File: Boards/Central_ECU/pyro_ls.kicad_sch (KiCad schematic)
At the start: 9 parts, among them Q2 DMT12H060LFDF-7

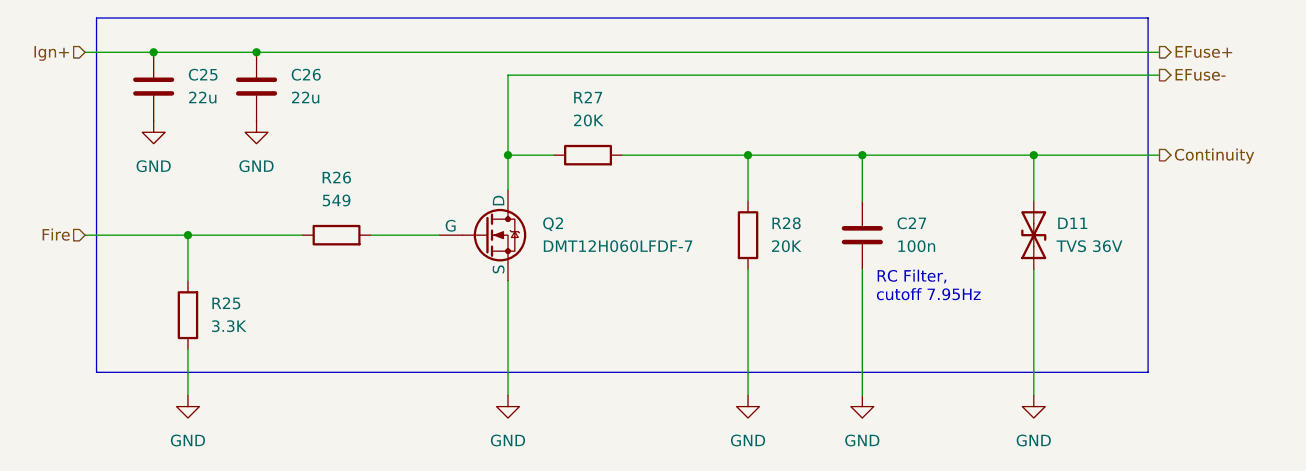
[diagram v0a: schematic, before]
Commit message: Added most connectors and hooking up
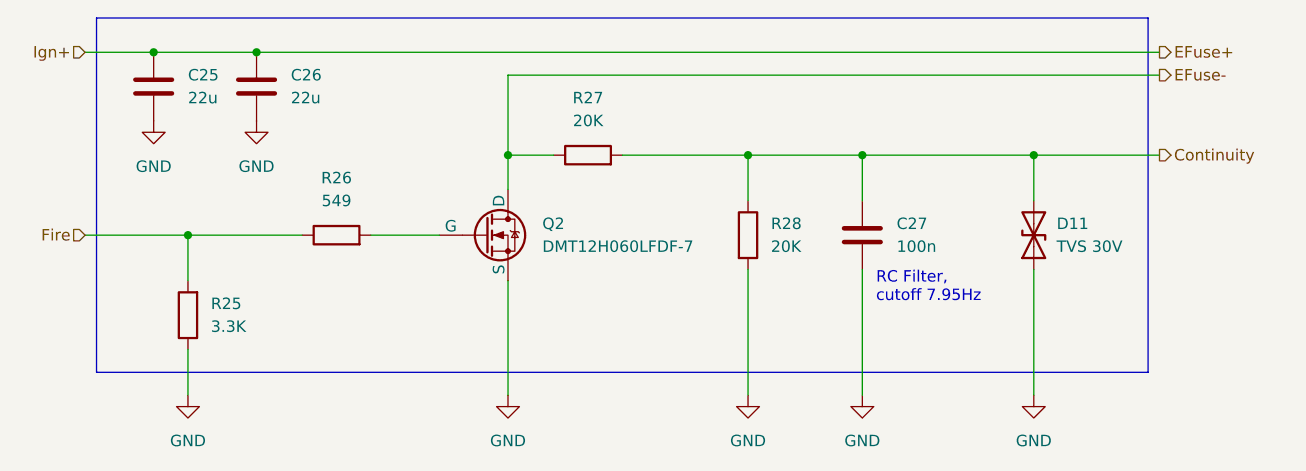
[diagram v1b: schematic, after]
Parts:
- D11: value TVS 36V -> TVS 30V; footprint Diode_SMD:D_SOD-523 -> Diode_SMD:D_SOD-882; MPN PJSD36TS_R1_00001 -> PESD1CANFD30LS-QYL
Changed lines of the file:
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@@
 			)
 		)
-		(property "Value" "TVS 36V"
+		(property "Value" "TVS 30V"
 			(at 259.08 143.51 90)
 			(effects
@@
 			)
 		)
-		(property "Footprint" "Diode_SMD:D_SOD-523"
+		(property "Footprint" "Diode_SMD:D_SOD-882"
 			(at 256.54 142.24 0)
 			(effects
@@
 			)
 		)
-		(property "Datasheet" "https://www.digikey.co.nz/en/products/detail/panjit-international-inc/PJSD36TS-R1-00001/14660198"
+		(property "Datasheet" "https://assets.nexperia.com/documents/data-sheet/PESD1CANFD30LS-Q.pdf"
 			(at 256.54 142.24 0)
 			(effects
@@
 			)
 		)
-		(property "MPN" "PJSD36TS_R1_00001"
+		(property "MPN" "PESD1CANFD30LS-QYL"
 			(at 256.54 142.24 90)
 			(effects

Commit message: For review
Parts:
- removed Q2: DMT12H060LFDF-7, Package_DFN_QFN:Diodes_UDFN2020-6_Type-F, symbol Simulation_SPICE:NMOS
- added Q2: DMT12H060LFDF, Package_DFN_QFN:Diodes_UDFN2020-6_Type-F, symbol TS_Symbols:DMT12H060LFDF
- D7: renamed from D11; MPN PESD1CANFD30LS-QYL -> PESD1CANFD30L-QYL
- renumbered C25 to C30, C26 to C31, C27 to C32, R27 to R32, R26 to R33, R28 to R34, R25 to R35
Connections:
- net Continuity: no longer D7.2 (A2)
- net EFuse-: now also D7.2 (A2), Q2.1, Q2.2 (D), Q2.5 (D), Q2.6 (D), Q2.7 (D)
- net GND: now also Q2.4, Q2.8 (S)
- net at R33.2: now also Q2.3
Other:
- company: (none) -> Hybrid Test Stand 2025
- title: (none) -> Pyro Low Side
- moved on the sheet: C32, D7, R32, R34

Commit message: Changed to 0603 passives and added NRST line
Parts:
- C30, C31, C32: footprint Capacitor_SMD:C_0805_2012Metric -> Capacitor_SMD:C_0603_1608Metric
- R32, R33, R34, R35: footprint Resistor_SMD:R_0805_2012Metric -> Resistor_SMD:R_0603_1608Metric
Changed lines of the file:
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@@
 			)
 		)
-		(property "Footprint" "Resistor_SMD:R_0805_2012Metric"
+		(property "Footprint" "Resistor_SMD:R_0603_1608Metric"
 			(at 240.792 142.24 90)
 			(effects
@@
 			)
 		)
-		(property "Footprint" "Resistor_SMD:R_0805_2012Metric"
+		(property "Footprint" "Resistor_SMD:R_0603_1608Metric"
 			(at 232.41 135.128 90)
 			(effects
@@
 			)
 		)
-		(property "Footprint" "Capacitor_SMD:C_0805_2012Metric"
+		(property "Footprint" "Capacitor_SMD:C_0603_1608Metric"
 			(at 159.7152 129.54 0)
 			(effects
@@
 			)
 		)
-		(property "Footprint" "Resistor_SMD:R_0805_2012Metric"
+		(property "Footprint" "Resistor_SMD:R_0603_1608Metric"
 			(at 179.07 144.018 90)
 			(effects
@@
 			)
 		)
-		(property "Footprint" "Resistor_SMD:R_0805_2012Metric"
+		(property "Footprint" "Resistor_SMD:R_0603_1608Metric"
 			(at 164.338 151.13 90)
 			(effects
@@
 			)
 		)
-		(property "Footprint" "Capacitor_SMD:C_0805_2012Metric"
+		(property "Footprint" "Capacitor_SMD:C_0603_1608Metric"
 			(at 256.2352 146.05 0)
 			(effects
@@
 			)
 		)
-		(property "Footprint" "Capacitor_SMD:C_0805_2012Metric"
+		(property "Footprint" "Capacitor_SMD:C_0603_1608Metric"
 			(at 171.1452 129.54 0)
 			(effects

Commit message: More progress on layout
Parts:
- C30, C31: footprint Capacitor_SMD:C_0603_1608Metric -> Capacitor_SMD:C_1206_3216Metric
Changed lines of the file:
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@@
 			)
 		)
-		(property "Footprint" "Capacitor_SMD:C_0603_1608Metric"
+		(property "Footprint" "Capacitor_SMD:C_1206_3216Metric"
 			(at 159.7152 129.54 0)
 			(effects
@@
 			)
 		)
-		(property "Footprint" "Capacitor_SMD:C_0603_1608Metric"
+		(property "Footprint" "Capacitor_SMD:C_1206_3216Metric"
 			(at 171.1452 129.54 0)
 			(effects

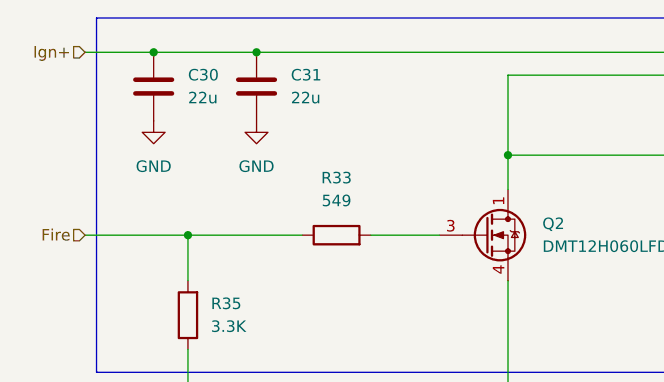
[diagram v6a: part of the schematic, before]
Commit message: Central ECU to order
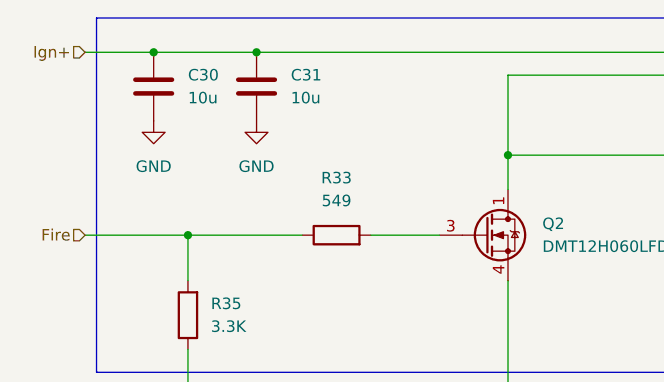
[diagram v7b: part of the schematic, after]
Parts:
- C30, C31: value 22u -> 10u
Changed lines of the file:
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@@
 			)
 		)
-		(property "Value" "22u"
+		(property "Value" "10u"
 			(at 162.56 126.9999 0)
 			(effects
@@
 			)
 		)
-		(property "Value" "22u"
+		(property "Value" "10u"
 			(at 173.99 126.9999 0)
 			(effects
